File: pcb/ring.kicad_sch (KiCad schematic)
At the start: 2 parts

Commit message: pcb
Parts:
- removed MK1: ICS-43434, Sensor_Audio:InvenSense_ICS-43434-6_3.5x2.65mm, symbol Sensor_Audio:ICS-43434
- added C1, C11, C3, C6, C9: 100n, Capacitor_SMD:C_0402_1005Metric, symbol Device:C_Small
- added C10, C4: 10u, Capacitor_SMD:C_0603_1608Metric, symbol Device:C_Small
- added C2, C8: 4.7u, Capacitor_SMD:C_0603_1608Metric, symbol Device:C_Small
- added C5: 100nF, Capacitor_SMD:C_0402_1005Metric, symbol Device:C_Small
- added C7: 1u, Capacitor_SMD:C_0402_1005Metric, symbol Device:C_Small
- added L1: 2.2u, Capacitor_SMD:C_0603_1608Metric, symbol Device:L
- added R1, R4: 100k, Resistor_SMD:R_0402_1005Metric, symbol Device:R
- added R2, R5: 10k, Resistor_SMD:R_0402_1005Metric, symbol Device:R
- added R3: 200k, Resistor_SMD:R_0402_1005Metric, symbol Device:R
- added U1: TMP117xxDRV, Package_SON:WSON-6-1EP_2x2mm_P0.65mm_EP1x1.6mm, symbol Sensor_Temperature:TMP117xxDRV
- added U2: TLV62569DBV, Package_TO_SOT_SMD:SOT-23-5, symbol Regulator_Switching:TLV62569DBV
- added U3: LSM6DSOXTR, Package_LGA:LGA-14_3x2.5mm_P0.5mm_LayoutBorder3x4y, symbol library:LSM6DSOXTR
- added U4: MAX30102, OptoDevice:Maxim_OLGA-14_3.3x5.6mm_P0.8mm, symbol Sensor:MAX30102
- renumbered MK2 to MK1
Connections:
- net GND: now also MK1.2 (LR), C1.1, C10.1, C11.2, C2.2, C3.1, C4.2, C5.2, C6.1, C7.1, C8.1, C9.2, R1.2, R4.2, U1.2 (GND), U1.4 (ADD0), U2.2 (GND), U3.1 (SDO/SA0), U3.2 (SDX), U3.3 (SCX), U3.6 (GND), U3.7 (GND__1), U4.12 (GND), U4.4 (PGND)
- net I2S_WC: now reaches MK1.1 (WS)
- net I2S_SCK: now reaches MK1.4 (SCK)
- net VDD: now reaches MK1.5 (VDD)
- net VDD: now also C1.2, C3.2, C4.1, C6.2, C7.2, C8.2, C9.1, L1.2, R2.2, R3.1, R5.2, U1.5 (V+), U3.12 (CS), U3.8 (VDD), U4.11 (VDD)
- net I2S_SD: now reaches MK1.6 (SD)
- net I2S_SD: now also R1.1
- new net: L1.1, U2.3 (SW)
- new net: R3.2, R4.1, U2.5 (FB)
- new net: R2.1, U1.3 (ALERT)
- new net: C5.1, U3.5 (VDDIO)
- new net +BATT: C10.2, C11.1, C2.1, U2.1 (EN), U2.4 (VIN), U4.10 (VLED+), U4.9 (VLED+)
- new net HBT_INT: R5.1, U4.13 (~{INT})
- new net I2C_SCL: U1.1 (SCL), U3.13 (SCL), U4.2 (SCL)
- new net I2C_SDA: U1.6 (SDA), U3.14 (SDA), U4.3 (SDA)
- new net IMU_INT1: U3.4 (INT1)
- new net IMU_INT2: U3.9 (INT2)
- no-connect marks 0 -> 2
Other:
- moved on the sheet: MK1

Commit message: schematic basically done
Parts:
- removed C1: 100n, Capacitor_SMD:C_0402_1005Metric, symbol Device:C_Small
- removed MK1: ICS-43434, Sensor_Audio:InvenSense_ICS-43434-6_3.5x2.65mm, symbol Sensor_Audio:ICS-43434
- removed U2: TLV62569DBV, Package_TO_SOT_SMD:SOT-23-5, symbol Regulator_Switching:TLV62569DBV
- added AE1: Antenna_Chip, symbol Device:Antenna_Chip
- added C12: 1.6p, Capacitor_SMD:C_0201_0603Metric, symbol Device:C_Small
- added C13: 18p, Capacitor_SMD:C_0201_0603Metric, symbol Device:C_Small
- added C14, C20, C22, C29, C30: 1u, Capacitor_SMD:C_0402_1005Metric, symbol Device:C_Small
- added C15, C16: C, Capacitor_SMD:C_0201_0603Metric, symbol Device:C_Small
- added C17: 10u, Capacitor_SMD:C_0402_1005Metric, symbol Device:C_Small
- added C18, C19, C23, C26: 100n, Capacitor_SMD:C_0201_0603Metric, symbol Device:C_Small
- added C21: 10n, Capacitor_SMD:C_0201_0603Metric, symbol Device:C_Small
- added C24, C31: 100n, Capacitor_SMD:C_0402_1005Metric, symbol Device:C_Small
- added C25, C32: 120p, Capacitor_SMD:C_0402_1005Metric, symbol Device:C_Small
- added FB1, FB2: BLM18AG102SN1, symbol Device:FerriteBead_Small
- added IC1: EFR32BG27C140F768IM32-B, Package_DFN_QFN:QFN-32-1EP_4x4mm_P0.4mm_EP2.9x2.9mm, symbol library:EFR32BG27C140F768IM32-B
- added L2: 2.0n, symbol Device:L
- added L3: 3.2n, symbol Device:L
- added MK2: IM69D130, Sensor_Audio:Infineon_PG-LLGA-5-1, symbol Sensor_Audio:IM69D130
- added R6: R, Resistor_SMD:R_0201_0603Metric, symbol Device:R
- added TP1: RST, symbol Connector:TestPoint
- added TP2: SWDIO, symbol Connector:TestPoint
- added TP3: SWCLK, symbol Connector:TestPoint
- added TP4: GND, symbol Connector:TestPoint
- added U6: TLV62569ADRL, Package_TO_SOT_SMD:SOT-563, symbol Regulator_Switching:TLV62569ADRL
- added Y1: 40MHz, symbol Device:Crystal_GND23_Small
- C10, C8: footprint Capacitor_SMD:C_0603_1608Metric -> Capacitor_SMD:C_0402_1005Metric
- C11, C6, C9: footprint Capacitor_SMD:C_0402_1005Metric -> Capacitor_SMD:C_0201_0603Metric
- C3: footprint Capacitor_SMD:C_0402_1005Metric -> Resistor_SMD:R_0201_0603Metric
- L1: footprint Capacitor_SMD:C_0603_1608Metric -> (none)
- R1: value 100k -> R; footprint Resistor_SMD:R_0402_1005Metric -> Resistor_SMD:R_0201_0603Metric
- R2, R5: footprint Resistor_SMD:R_0402_1005Metric -> Resistor_SMD:R_0201_0603Metric
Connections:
- net I2S_SD is gone; now on net I2C_SCL: R1.1
- net +BATT: now also U6.3 (VIN), U6.5 (EN)
- net GND: now also AE1.1 (FEED), C12.2, C14.1, C15.1, C16.2, C17.1, C18.2, C19.2, C20.1, C21.2, C22.1, C23.2, C24.2, C25.2, C26.1, C29.2, C30.2, C31.2, C32.2, IC1.11 (RFVSS), IC1.27 (VREGVSS), IC1.33 (VSS), MK2.4 (SELECT), MK2.5 (GND), TP4.1, U6.2 (GND), Y1.2, Y1.3; no longer R1.2
- net HBT_INT: now also IC1.16 (PB00)
- net I2C_SDA: now also R6.1
- net IMU_INT1: now also IC1.15 (PB01)
- net IMU_INT2: now also IC1.14 (PB02)
- net VDD: now also R1.2, C17.2, C18.1, C19.1, C20.2, C21.1, C22.2, C23.1, C26.2, FB1.1, FB2.1, IC1.26 (VREGVDD), IC1.28 (DVDD), IC1.29 (AVDD), IC1.30 (IOVDD), MK2.2 (VDD), R6.2
- net at L1.1: now also U6.4 (SW)
- net at R3.2, R4.1: now also U6.1 (FB)
- net TMP_INT: now reaches R2.1, U1.3 (ALERT)
- net TMP_INT: now also IC1.17 (PA00)
- new net: C30.1, C31.1, C32.1, FB2.2, IC1.13 (PAVDD)
- new net: C12.1, L2.2, L3.1
- new net: C13.1, L3.2
- new net: C24.1, C25.1, C29.1, FB1.2, IC1.10 (RFVDD)
- new net: IC1.18 (PA01), TP3.1
- new net: IC1.19 (PA02), TP2.1
- new net: C14.2, IC1.24 (DECOUPLE)
- new net: C15.2, IC1.7 (HFXTAL_I), Y1.4
- new net: C16.1, IC1.8 (HFXTAL_O), Y1.1
- new net: IC1.9 (RESETN), TP1.1
- new net: AE1.2 (PCB_Trace), C13.2
- new net MIC_CLOCK: MK2.3 (CLOCK)
- new net MIC_DATA: MK2.1 (DATA)
- new net RF: IC1.12 (RF2G4_IO), L2.1
- no-connect marks 2 -> 3
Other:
- note added: "250 uA max"
- note added: "550 uA max"
- note added: "600 uA typ; 1200 uA max"
- note added: "LED draws 20-50 mA"

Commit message: ldo
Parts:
- removed C2: 4.7u, Capacitor_SMD:C_0603_1608Metric, symbol Device:C_Small
- removed C4: 10u, Capacitor_SMD:C_0603_1608Metric, symbol Device:C_Small
- removed L1: 2.2u, symbol Device:L
- removed R3: 200k, Resistor_SMD:R_0402_1005Metric, symbol Device:R
- removed R4: 100k, Resistor_SMD:R_0402_1005Metric, symbol Device:R
- removed U6: TLV62569ADRL, Package_TO_SOT_SMD:SOT-563, symbol Regulator_Switching:TLV62569ADRL
- added C27, C28: 1u, Capacitor_SMD:C_0402_1005Metric, symbol Device:C_Small
- added U2: TPS7A20xxxDQN, Package_SON:Texas_X2SON-4_1x1mm_P0.65mm, symbol Regulator_Linear:TPS7A20xxxDQN
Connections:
- net +BATT: now also C27.1, U2.3 (EN), U2.4 (IN)
- net GND: now also C27.2, C28.2, U2.2 (GND), U2.5 (Pad)
- net VDD: now also C28.1, U2.1 (OUT)

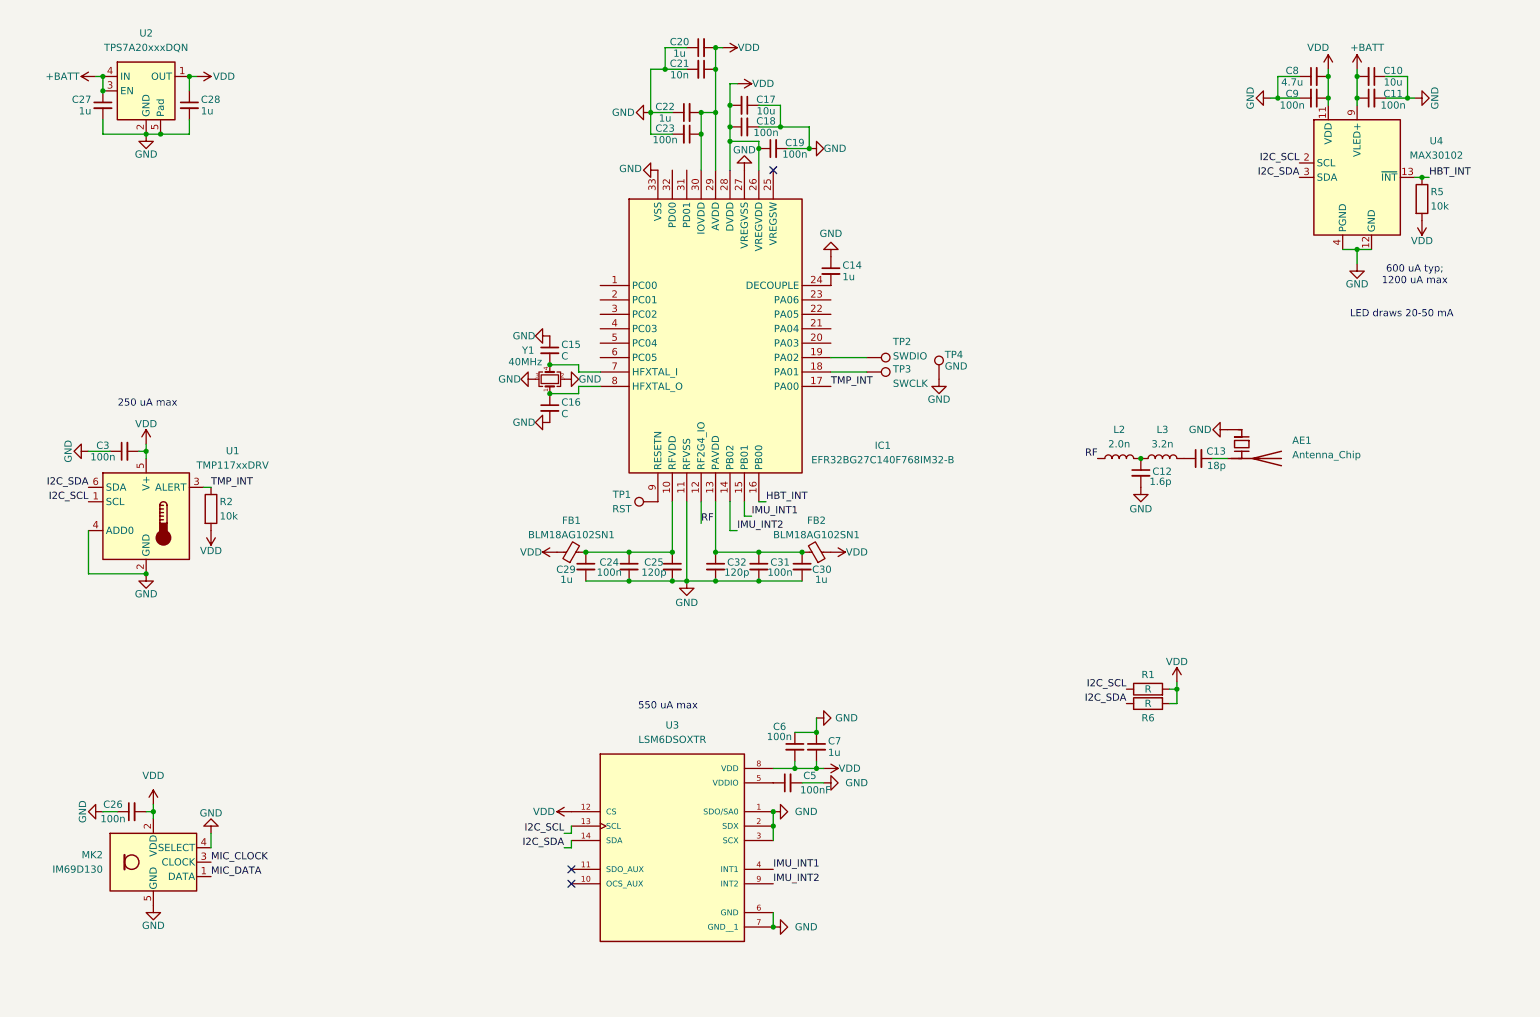
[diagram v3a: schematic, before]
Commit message: battery protection
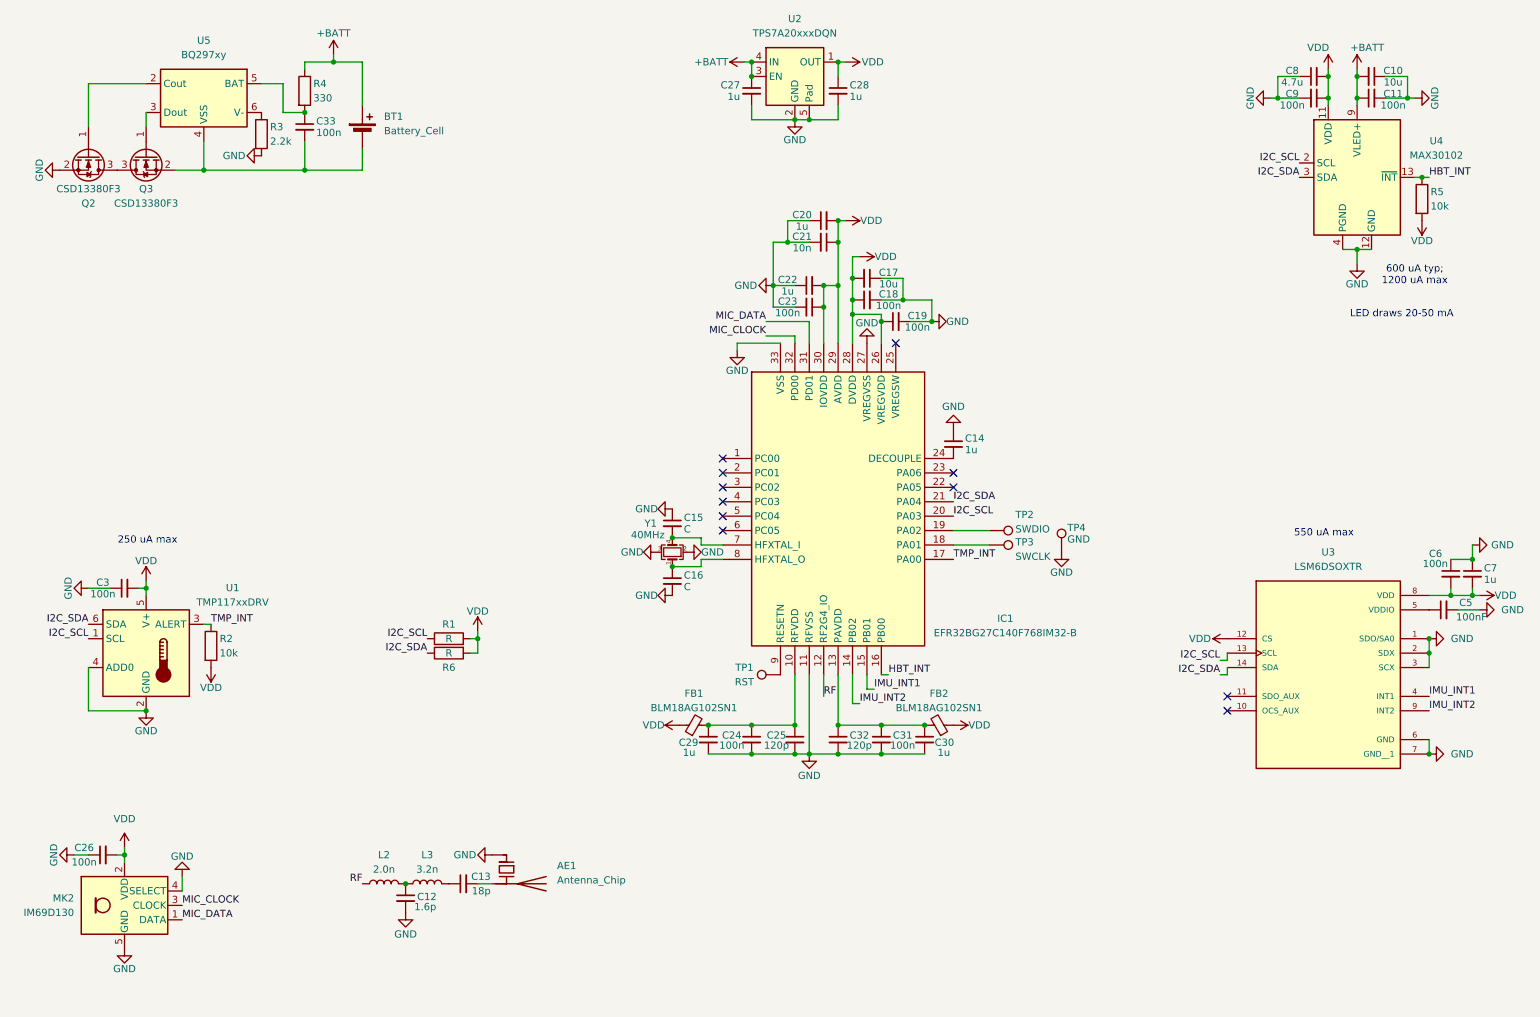
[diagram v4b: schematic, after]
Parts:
- added BT1: Battery_Cell, symbol Device:Battery_Cell
- added C33: 100n, Capacitor_SMD:C_0201_0603Metric, symbol Device:C_Small
- added Q2, Q3: CSD13380F3, Package_DFN_QFN:Texas_PicoStar_DFN-3_0.69x0.60mm, symbol Transistor_FET:CSD13380F3
- added R3: 2.2k, Capacitor_SMD:C_0201_0603Metric, symbol Device:R
- added R4: 330, Capacitor_SMD:C_0201_0603Metric, symbol Device:R
- added U5: BQ297xy, Package_SON:WSON-6_1.5x1.5mm_P0.5mm, symbol Battery_Management:BQ297xy
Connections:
- net +BATT: now also BT1.1 (+), R4.1
- net GND: now also Q2.2 (S), R3.2
- net I2C_SCL: now also IC1.20 (PA03)
- net I2C_SDA: now also IC1.21 (PA04)
- net MIC_CLOCK: now also IC1.32 (PD00)
- net MIC_DATA: now also IC1.31 (PD01)
- new net: Q2.1 (G), U5.2 (Cout)
- new net: Q2.3 (D), Q3.3 (D)
- new net: Q3.1 (G), U5.3 (Dout)
- new net: BT1.2 (-), C33.2, Q3.2 (S), U5.4 (VSS)
- new net: C33.1, R4.2, U5.5 (BAT)
- new net: R3.1, U5.6 (V-)
- no-connect marks 3 -> 11
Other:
- moved on the sheet: AE1, C12, C13, C14, C15, C16, C17, C18, C19, C20, C21, C22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

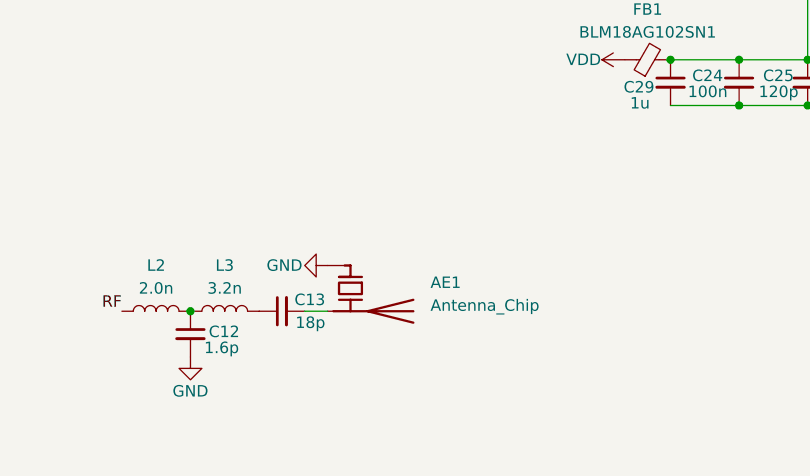
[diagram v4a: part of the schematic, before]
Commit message: switched to smaller battery, will be removing external protection
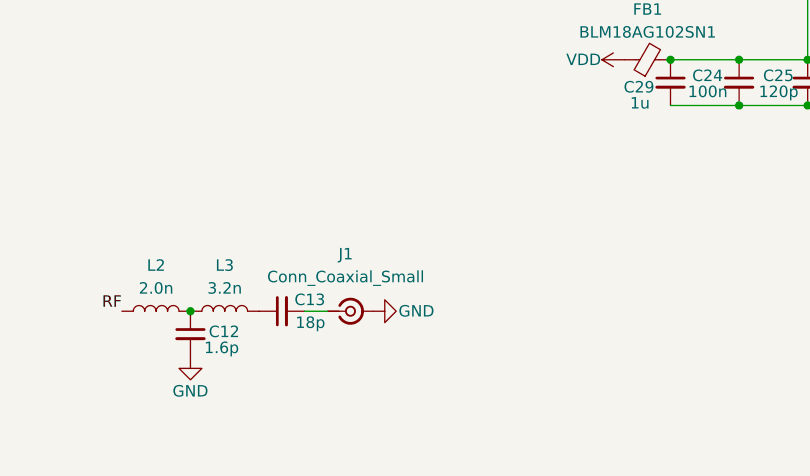
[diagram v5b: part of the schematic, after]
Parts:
- removed AE1: Antenna_Chip, symbol Device:Antenna_Chip
- added J1: Conn_Coaxial_Small, Connector_Coaxial:U.FL_Hirose_U.FL-R-SMT-1_Vertical, symbol Connector:Conn_Coaxial_Small
- BT1: footprint (none) -> library:Battery
- C24, C25, C31, C32, C5: footprint Capacitor_SMD:C_0402_1005Metric -> Capacitor_SMD:C_0201_0603Metric
- L2, L3: footprint (none) -> Inductor_SMD:L_0201_0603Metric
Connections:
- net GND: now also J1.2 (Ext)
- net at C13.2: now also J1.1 (In)
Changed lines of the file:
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@@
 	(symbol
 		(lib_id "power:GND")
-		(at 101.6 170.18 270)
+		(at 106.68 175.26 90)
 		(unit 1)
 		(exclude_from_sim no)
@@
 		(dnp no)
 		(property "Reference" "#PWR027"
-			(at 95.25 170.18 0)
+			(at 113.03 175.26 0)
 			(hide yes)
 			(effects
@@
 		)
 		(property "Value" "GND"
-			(at 98.806 170.18 90)
+			(at 109.474 175.26 90)
 			(effects
 				(font
@@
 		)
 		(property "Footprint" ""
-			(at 101.6 170.18 0)
+			(at 106.68 175.26 0)
 			(hide yes)
 			(effects
@@
 		)
 		(property "Datasheet" ""
-			(at 101.6 170.18 0)
+			(at 106.68 175.26 0)
 			(hide yes)
 			(effects
@@
 		)
 		(property "Description" "Power symbol creates a global label with name \"GND\" , ground"
-			(at 101.6 170.18 0)
+			(at 106.68 175.26 0)
 			(hide yes)
 			(effects
@@
 	)
 	(symbol
+		(lib_id "Connector:Conn_Coaxial_Small")
+		(at 104.14 175.26 0)
+		(unit 1)
+		(exclude_from_sim no)
+		(in_bom yes)
+		(on_board yes)
+		(dnp no)
+		(fields_autoplaced yes)
+		(property "Reference" "J1"
+			(at 103.6204 168.91 0)
+			(effects
+				(font
+					(size 1.27 1.27)
+				)
+			)
+		)
+		(property "Value" "Conn_Coaxial_Small"
+			(at 103.6204 171.45 0)
+			(effects
+				(font
+					(size 1.27 1.27)
+				)
+			)
+		)
+		(property "Footprint" "Connector_Coaxial:U.FL_Hirose_U.FL-R-SMT-1_Vertical"
+			(at 104.14 175.26 0)
+			(hide yes)
+			(effects
+				(font
+					(size 1.27 1.27)
+				)
+			)
+		)
+		(property "Datasheet" "~"
+			(at 104.14 175.26 0)
+			(hide yes)
+			(effects
+				(font
+					(size 1.27 1.27)
+				)
+			)
+		)
+		(property "Description" "small coaxial connector (BNC, SMA, SMB, SMC, Cinch/RCA, LEMO, ...)"
+			(at 104.14 175.26 0)
+			(hide yes)
+			(effects
+				(font
+					(size 1.27 1.27)
+				)
+			)
+		)
+		(pin "2"
+		)
+		(pin "1"
+		)
+		(instances
+			(project ""
+				(path "/d55284dd-9e0b-472d-90fe-626f8af64020"
+					(reference "J1")
+					(unit 1)
+				)
+			)
+		)
+	)
+	(symbol
 		(lib_id "power:GND")
 		(at 179.07 76.2 90)
@@
 			)
 		)
-		(property "Footprint" ""
+		(property "Footprint" "Inductor_SMD:L_0201_0603Metric"
 			(at 90.17 175.26 0)
 			(hide yes)
@@
 			)
 		)
-		(property "Footprint" ""
+		(property "Footprint" "library:Battery"
 			(at 78.74 41.656 90)
 			(hide yes)
@@
 	)
 	(symbol
-		(lib_id "Device:Antenna_Chip")
-		(at 104.14 172.72 270)
-		(unit 1)
-		(exclude_from_sim no)
-		(in_bom yes)
-		(on_board yes)
-		(dnp no)
-		(fields_autoplaced yes)
-		(property "Reference" "AE1"
-			(at 113.03 172.0849 90)
-			(effects
-				(font
-					(size 1.27 1.27)
-				)
-				(justify left)
-			)
-		)
-		(property "Value" "Antenna_Chip"
-			(at 113.03 174.6249 90)
-			(effects
-				(font
-					(size 1.27 1.27)
-				)
-				(justify left)
-			)
-		)
-		(property "Footprint" ""
-			(at 108.585 170.18 0)
-			(hide yes)
-			(effects
-				(font
-					(size 1.27 1.27)
-				)
-			)
-		)
-		(property "Datasheet" "~"
-			(at 108.585 170.18 0)
-			(hide yes)
-			(effects
-				(font
-					(size 1.27 1.27)
-				)
-			)
-		)
-		(property "Description" "Ceramic chip antenna with pin for PCB trace"
-			(at 104.14 172.72 0)
-			(hide yes)
-			(effects
-				(font
-					(size 1.27 1.27)
-				)
-			)
-		)
-		(pin "1"
-		)
-		(pin "2"
-		)
-		(instances
-			(project ""
-				(path "/d55284dd-9e0b-472d-90fe-626f8af64020"
-					(reference "AE1")
-					(unit 1)
-				)
-			)
-		)
-	)
-	(symbol
 		(lib_id "Device:C_Small")
 		(at 154.94 149.86 0)
@@
 			)
 		)
-		(property "Footprint" "Capacitor_SMD:C_0402_1005Metric"
+		(property "Footprint" "Capacitor_SMD:C_0201_0603Metric"
 			(at 154.94 149.86 0)
 			(hide yes)
@@
 			)
 		)
-		(property "Footprint" ""
+		(property "Footprint" "Inductor_SMD:L_0201_0603Metric"
 			(at 82.55 175.26 0)
 			(hide yes)
@@
 			)
 		)
-		(property "Footprint" "Capacitor_SMD:C_0402_1005Metric"
+		(property "Footprint" "Capacitor_SMD:C_0201_0603Metric"
 			(at 170.18 149.86 0)
 			(hide yes)
@@
 			)
 		)
-		(property "Footprint" "Capacitor_SMD:C_0402_1005Metric"
+		(property "Footprint" "Capacitor_SMD:C_0201_0603Metric"
 			(at 269.24 127 0)
 			(hide yes)
@@
 			)
 		)
-		(property "Footprint" "Capacitor_SMD:C_0402_1005Metric"
+		(property "Footprint" "Capacitor_SMD:C_0201_0603Metric"
 			(at 162.56 149.86 0)
 			(hide yes)
@@
 			)
 		)
-		(property "Footprint" "Capacitor_SMD:C_0402_1005Metric"
+		(property "Footprint" "Capacitor_SMD:C_0201_0603Metric"
 			(at 147.32 149.86 0)
 			(hide yes)

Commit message: pcb laid out, schematic done
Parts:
- removed C15, C16: C, Capacitor_SMD:C_0201_0603Metric, symbol Device:C_Small
- removed TP4: GND, symbol Connector:TestPoint
- removed Y1: 40MHz, symbol Device:Crystal_GND23_Small
- added C34: 1u, Capacitor_SMD:C_0201_0603Metric, symbol Device:C_Small
- added C4: 2.2u, Resistor_SMD:R_0201_0603Metric, symbol Device:C_Small
- added D1: ESD9B5.0ST5G, Diode_SMD:D_SOD-923, symbol Diode:ESD9B5.0ST5G
- added D4, D5: ESD9B3.3ST5G, Diode_SMD:D_SOD-923, symbol Diode:ESD9B3.3ST5G
- added R7: 10k, Resistor_SMD:R_0201_0603Metric, symbol Device:R
- added R8: 100k, Resistor_SMD:R_0201_0603Metric, symbol Device:R
- added TP5: +, TestPoint:TestPoint_Pad_D1.5mm, symbol Connector:TestPoint
- added TP6, TP7: -, TestPoint:TestPoint_Pad_D1.0mm, symbol Connector:TestPoint
- added U6: BQ27427YZFR, Package_BGA:BGA-9_1.6x1.6mm_Layout3x3_P0.5mm, symbol library:BQ27427YZFR
- added Y2: 38.4MHz, Crystal:Crystal_SMD_1210-4Pin_1.2x1.0mm, symbol Device:Crystal_GND24_Small
- FB1, FB2: footprint (none) -> Inductor_SMD:L_0603_1608Metric
- J1: footprint Connector_Coaxial:U.FL_Hirose_U.FL-R-SMT-1_Vertical -> RF_Antenna:Texas_SWRA117D_2.4GHz_Right
- R2, R5: value 10k -> 100k
- TP2, TP3: footprint (none) -> TestPoint:TestPoint_Pad_D1.0mm
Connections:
- net +BATT: now also C34.1, D1.1 (A1), TP5.1, U6.C3 (BAT)
- net GND: now also C34.2, C4.1, D1.2 (A2), D4.2 (A2), D5.1 (A1), R7.2, TP6.1, TP7.1, U6.B2 (VSS), U6.C1 (VSS), Y2.2, Y2.4
- net HBT_INT: now also IC1.1 (PC00); no longer IC1.16 (PB00)
- net I2C_SCL: now also U6.A3 (SCL)
- net I2C_SDA: now also U6.A2 (SDA)
- net IMU_INT1: now also IC1.3 (PC02); no longer IC1.15 (PB01)
- net IMU_INT2: now also IC1.5 (PC04); no longer IC1.14 (PB02)
- net MIC_CLOCK: now also IC1.31 (PD01); no longer IC1.32 (PD00)
- net MIC_DATA: now also IC1.32 (PD00); no longer IC1.31 (PD01)
- net VDD: now also C5.1, U3.5 (VDDIO), R8.2, U6.C2 (SRX)
- net at IC1.18 (PA01), TP3.1: now also D5.2 (A2)
- net at IC1.19 (PA02), TP2.1: now also D4.1 (A1)
- net at IC1.7 (HFXTAL_I): now also Y2.3
- net at IC1.8 (HFXTAL_O): now also Y2.1
- new net: R7.1, U6.B1 (BIN)
- new net: C4.2, U6.B3 (VDD)
- new net BAT_LOW: R8.1, U6.A1 (GPOUT)
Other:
- moved on the sheet: TP2, TP3
